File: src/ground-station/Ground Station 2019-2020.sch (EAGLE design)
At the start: 17 parts, among them U1 ADAFRUIT_RFM95W_LORA_RADIO

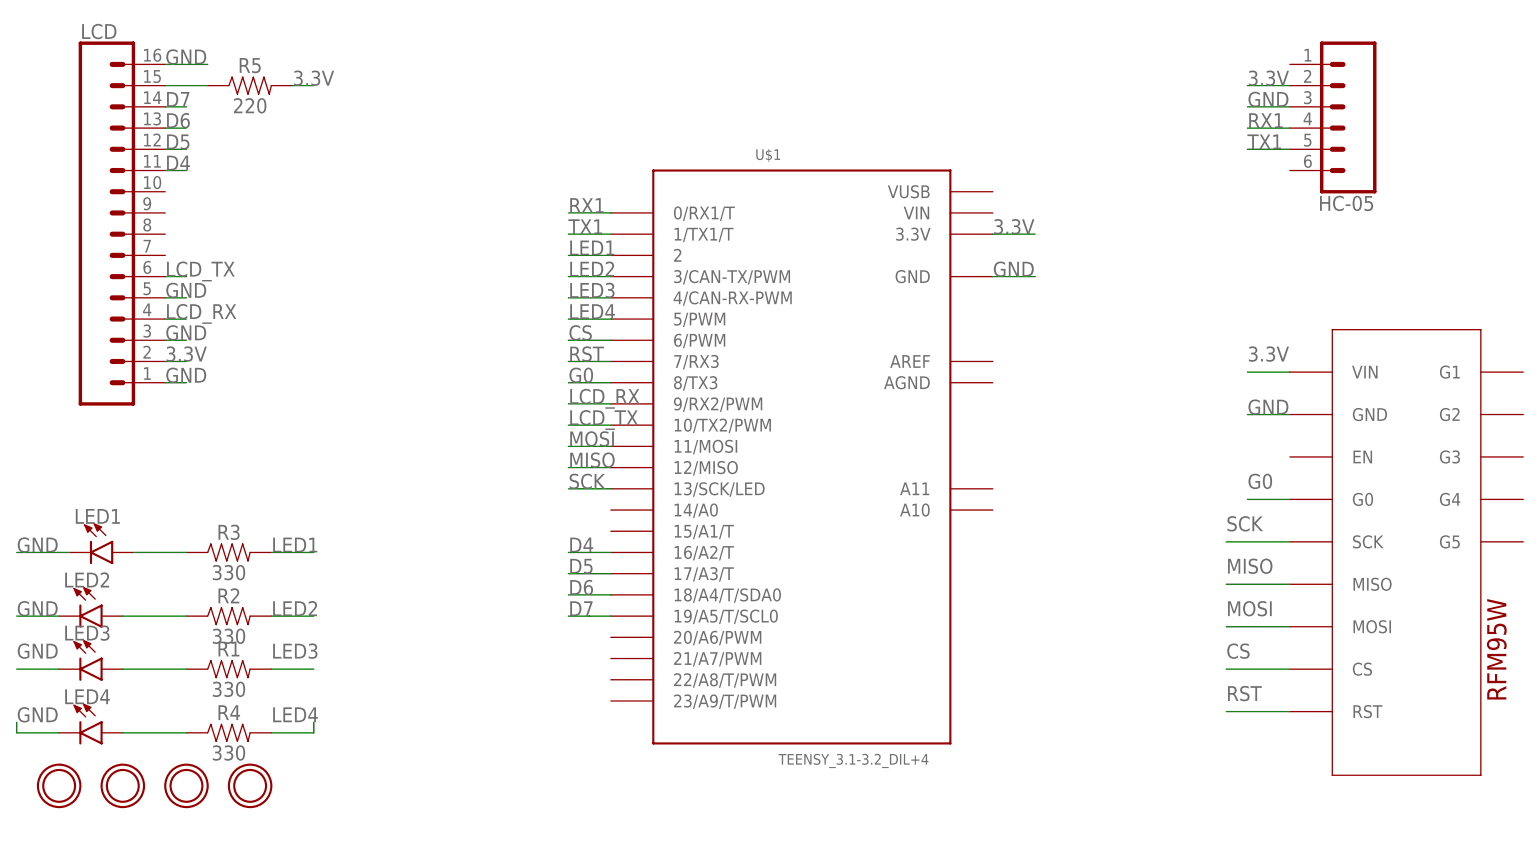
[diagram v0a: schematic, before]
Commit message: Changed LCD to OLED display, changed mounting holes.
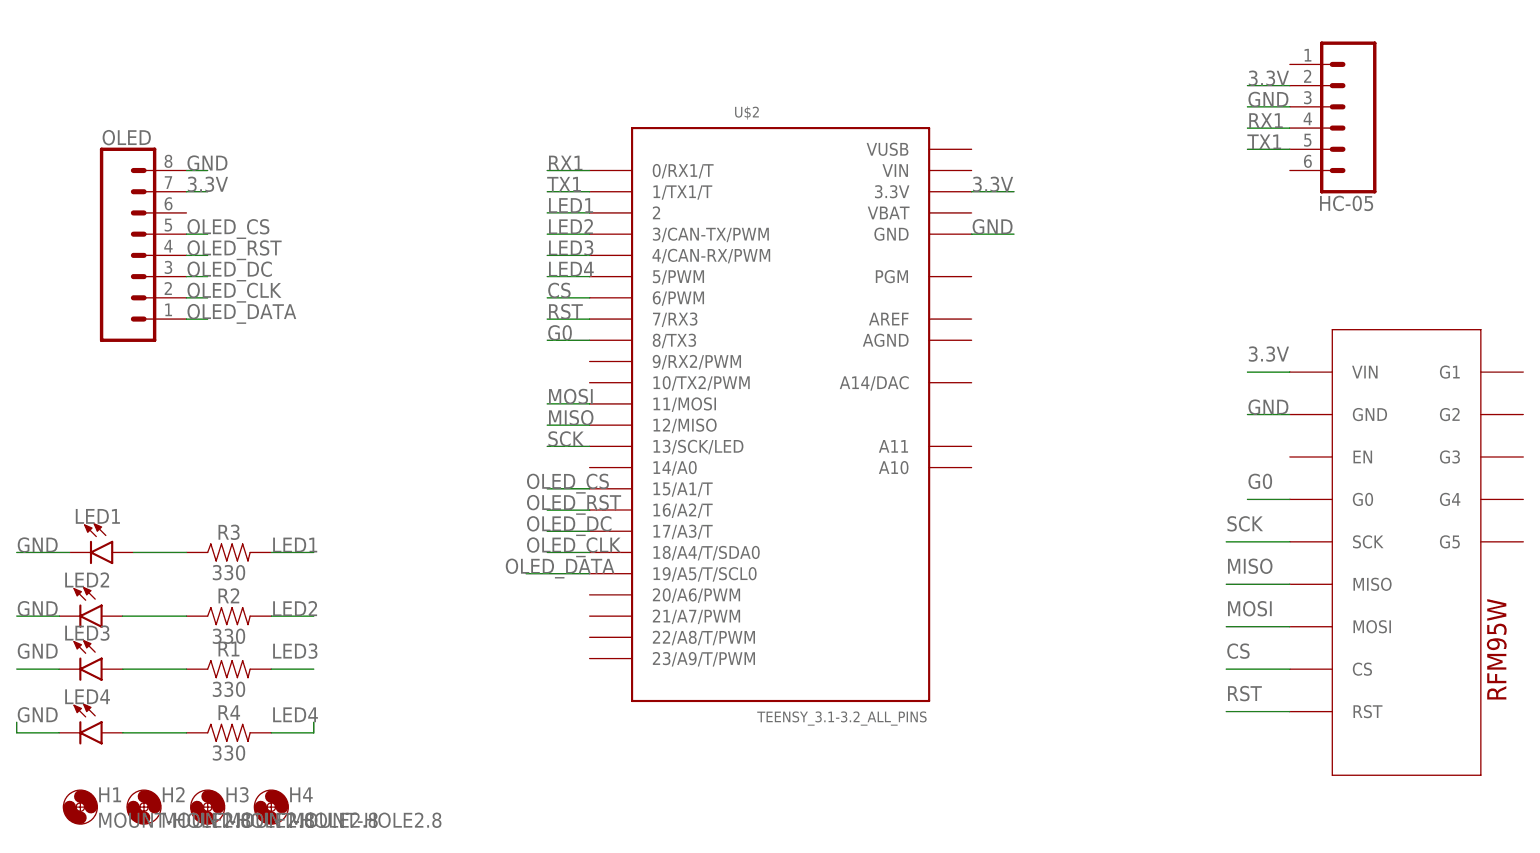
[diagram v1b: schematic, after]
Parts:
- removed LCD: (no value), SparkFun-Connectors:CONN_16
- removed R5: 220, SparkFun-Resistors:330OHM-HORIZ-1/10W-5%
- removed U$1: TEENSY_3.1-3.2_DIL+4, Teensy_3_and_LC_Series_Boards_v1.4:TEENSY_3.1-3.2_DIL+4
- removed U$3, U$4, U$5: MOUNTINGHOLE2.5, microbuilder:MOUNTINGHOLE2.5
- added H1, H2, H3, H4: MOUNT-HOLE2.8, holes:MOUNT-HOLE2.8
- added OLED: (no value), SparkFun-Connectors:CONN_08"
- U$2: value MOUNTINGHOLE2.5 -> TEENSY_3.1-3.2_ALL_PINS; device microbuilder:MOUNTINGHOLE2.5 -> Teensy_3_and_LC_Series_Boards_v1.4:TEENSY_3.1-3.2_ALL_PINS
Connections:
- removed net D4: LCD.11, U$1.16/A2/T
- removed net D5: LCD.12, U$1.17/A3/T
- removed net D6: LCD.13, U$1.18/A4/T/SDA0
- removed net D7: LCD.14, U$1.19/A5/T/SCL0
- removed net LCD_RX: LCD.4, U$1.9/RX2/PWM
- removed net LCD_TX: LCD.6, U$1.10/TX2/PWM
- removed net N$4: LCD.15, R5.1
- new net OLED_CLK: OLED.2, U$2.18/A4/T/SDA0
- new net OLED_CS: OLED.5, U$2.15/A1/T
- new net OLED_DATA: OLED.1, U$2.19/A5/T/SCL0
- new net OLED_DC: OLED.3, U$2.17/A3/T
- new net OLED_RST: OLED.4, U$2.16/A2/T
- net 3.3V: now also OLED.7, U$2.3.3V; no longer LCD.2, R5.2, U$1.3.3V
- net CS: now also U$2.6/PWM; no longer U$1.6/PWM
- net G0: now also U$2.8/TX3; no longer U$1.8/TX3
- net GND: now also OLED.8, U$2.GND; no longer LCD.1, LCD.16, LCD.3, LCD.5, U$1.GND
- net LED1: now also U$2.2; no longer U$1.2
- net LED2: now also U$2.3/CAN-TX/PWM; no longer U$1.3/CAN-TX/PWM
- net LED3: now also U$2.4/CAN-RX/PWM; no longer U$1.4/CAN-RX-PWM
- net LED4: now also U$2.5/PWM; no longer U$1.5/PWM
- net MISO: now also U$2.12/MISO; no longer U$1.12/MISO
- net MOSI: now also U$2.11/MOSI; no longer U$1.11/MOSI
- net RST: now also U$2.7/RX3; no longer U$1.7/RX3
- net RX1: now also U$2.0/RX1/T; no longer U$1.0/RX1/T
- net SCK: now also U$2.13/SCK/LED; no longer U$1.13/SCK/LED
- net TX1: now also U$2.1/TX1/T; no longer U$1.1/TX1/T

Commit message: Added Cam outputs
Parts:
- R1, R2, R3, R4: value 330 -> 220
- renumbered LED1 to RED, LED2 to YELLOW, LED3 to BLUE, LED4 to WHITE
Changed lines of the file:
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@@
 <part name="U1" library="AERO_Eagle_Library" deviceset="ADAFRUIT_RFM95W_LORA_RADIO" device=""/>
 <part name="HC-05" library="SparkFun-Connectors" library_urn="urn:adsk.eagle:library:513" deviceset="CONN_06" device="SILK_FEMALE_PTH" package3d_urn="urn:adsk.eagle:package:38009/1"/>
-<part name="LED1" library="SparkFun-LED" library_urn="urn:adsk.eagle:library:529" deviceset="LED" device="5MM" package3d_urn="urn:adsk.eagle:package:39353/1"/>
-<part name="LED2" library="SparkFun-LED" library_urn="urn:adsk.eagle:library:529" deviceset="LED" device="5MM" package3d_urn="urn:adsk.eagle:package:39353/1"/>
-<part name="LED3" library="SparkFun-LED" library_urn="urn:adsk.eagle:library:529" deviceset="LED" device="5MM" package3d_urn="urn:adsk.eagle:package:39353/1"/>
-<part name="R1" library="SparkFun-Resistors" library_urn="urn:adsk.eagle:library:532" deviceset="330OHM" device="-HORIZ-1/10W-5%" package3d_urn="urn:adsk.eagle:package:39658/1" value="330"/>
-<part name="R2" library="SparkFun-Resistors" library_urn="urn:adsk.eagle:library:532" deviceset="330OHM" device="-HORIZ-1/10W-5%" package3d_urn="urn:adsk.eagle:package:39658/1" value="330"/>
-<part name="R3" library="SparkFun-Resistors" library_urn="urn:adsk.eagle:library:532" deviceset="330OHM" device="-HORIZ-1/10W-5%" package3d_urn="urn:adsk.eagle:package:39658/1" value="330"/>
-<part name="R4" library="SparkFun-Resistors" library_urn="urn:adsk.eagle:library:532" deviceset="330OHM" device="-HORIZ-1/10W-5%" package3d_urn="urn:adsk.eagle:package:39658/1" value="330"/>
-<part name="LED4" library="SparkFun-LED" library_urn="urn:adsk.eagle:library:529" deviceset="LED" device="5MM" package3d_urn="urn:adsk.eagle:package:39353/1"/>
+<part name="RED" library="SparkFun-LED" library_urn="urn:adsk.eagle:library:529" deviceset="LED" device="5MM" package3d_urn="urn:adsk.eagle:package:39353/1"/>
+<part name="YELLOW" library="SparkFun-LED" library_urn="urn:adsk.eagle:library:529" deviceset="LED" device="5MM" package3d_urn="urn:adsk.eagle:package:39353/1"/>
+<part name="BLUE" library="SparkFun-LED" library_urn="urn:adsk.eagle:library:529" deviceset="LED" device="5MM" package3d_urn="urn:adsk.eagle:package:39353/1"/>
+<part name="R1" library="SparkFun-Resistors" library_urn="urn:adsk.eagle:library:532" deviceset="330OHM" device="-HORIZ-1/10W-5%" package3d_urn="urn:adsk.eagle:package:39658/1" value="220"/>
+<part name="R2" library="SparkFun-Resistors" library_urn="urn:adsk.eagle:library:532" deviceset="330OHM" device="-HORIZ-1/10W-5%" package3d_urn="urn:adsk.eagle:package:39658/1" value="220"/>
+<part name="R3" library="SparkFun-Resistors" library_urn="urn:adsk.eagle:library:532" deviceset="330OHM" device="-HORIZ-1/10W-5%" package3d_urn="urn:adsk.eagle:package:39658/1" value="220"/>
+<part name="R4" library="SparkFun-Resistors" library_urn="urn:adsk.eagle:library:532" deviceset="330OHM" device="-HORIZ-1/10W-5%" package3d_urn="urn:adsk.eagle:package:39658/1" value="220"/>
+<part name="WHITE" library="SparkFun-LED" library_urn="urn:adsk.eagle:library:529" deviceset="LED" device="5MM" package3d_urn="urn:adsk.eagle:package:39353/1"/>
 <part name="H1" library="holes" library_urn="urn:adsk.eagle:library:237" deviceset="MOUNT-HOLE" device="2.8" package3d_urn="urn:adsk.eagle:package:14271/1"/>
 <part name="H2" library="holes" library_urn="urn:adsk.eagle:library:237" deviceset="MOUNT-HOLE" device="2.8" package3d_urn="urn:adsk.eagle:package:14271/1"/>
@@
 <instance part="U1" gate="G$1" x="187.96" y="120.65" rot="R270"/>
 <instance part="HC-05" gate="G$1" x="187.96" y="147.32" rot="R180"/>
-<instance part="LED1" gate="G$1" x="41.91" y="93.98" rot="R270"/>
-<instance part="LED2" gate="G$1" x="40.64" y="86.36" rot="R270"/>
-<instance part="LED3" gate="G$1" x="40.64" y="80.01" rot="R270"/>
+<instance part="RED" gate="G$1" x="41.91" y="93.98" rot="R270"/>
+<instance part="YELLOW" gate="G$1" x="40.64" y="86.36" rot="R270"/>
+<instance part="BLUE" gate="G$1" x="40.64" y="80.01" rot="R270"/>
 <instance part="R1" gate="G$1" x="55.88" y="80.01"/>
 <instance part="R2" gate="G$1" x="55.88" y="86.36"/>
 <instance part="R3" gate="G$1" x="55.88" y="93.98"/>
 <instance part="R4" gate="G$1" x="55.88" y="72.39"/>
-<instance part="LED4" gate="G$1" x="40.64" y="72.39" rot="R270"/>
+<instance part="WHITE" gate="G$1" x="40.64" y="72.39" rot="R270"/>
 <instance part="H1" gate="G$1" x="38.1" y="63.5"/>
 <instance part="H2" gate="G$1" x="45.72" y="63.5"/>
@@
 </segment>
 <segment>
-<pinref part="LED3" gate="G$1" pin="C"/>
+<pinref part="BLUE" gate="G$1" pin="C"/>
 <wire x1="35.56" y1="80.01" x2="30.48" y2="80.01" width="0.1524" layer="91"/>
 <label x="30.48" y="81.28" size="1.778" layer="95"/>
 </segment>
 <segment>
-<pinref part="LED2" gate="G$1" pin="C"/>
+<pinref part="YELLOW" gate="G$1" pin="C"/>
 <wire x1="35.56" y1="86.36" x2="30.48" y2="86.36" width="0.1524" layer="91"/>
 <label x="30.48" y="86.36" size="1.778" layer="95"/>
 </segment>
 <segment>
-<pinref part="LED1" gate="G$1" pin="C"/>
+<pinref part="RED" gate="G$1" pin="C"/>
 <wire x1="36.83" y1="93.98" x2="30.48" y2="93.98" width="0.1524" layer="91"/>
 <label x="30.48" y="93.98" size="1.778" layer="95"/>
@@
 </segment>
 <segment>
-<pinref part="LED4" gate="G$1" pin="C"/>
+<pinref part="WHITE" gate="G$1" pin="C"/>
 <wire x1="35.56" y1="72.39" x2="30.48" y2="72.39" width="0.1524" layer="91"/>
 <wire x1="30.48" y1="72.39" x2="30.48" y2="73.66" width="0.1524" layer="91"/>
@@
 <segment>
 <pinref part="R1" gate="G$1" pin="1"/>
-<pinref part="LED3" gate="G$1" pin="A"/>
+<pinref part="BLUE" gate="G$1" pin="A"/>
 <wire x1="50.8" y1="80.01" x2="43.18" y2="80.01" width="0.1524" layer="91"/>
 </segment>
@@
 <segment>
 <pinref part="R2" gate="G$1" pin="1"/>
-<pinref part="LED2" gate="G$1" pin="A"/>
+<pinref part="YELLOW" gate="G$1" pin="A"/>
 <wire x1="50.8" y1="86.36" x2="43.18" y2="86.36" width="0.1524" layer="91"/>
 </segment>
@@
 <segment>
 <pinref part="R3" gate="G$1" pin="1"/>
-<pinref part="LED1" gate="G$1" pin="A"/>
+<pinref part="RED" gate="G$1" pin="A"/>
 <wire x1="50.8" y1="93.98" x2="44.45" y2="93.98" width="0.1524" layer="91"/>
 </segment>
@@
 <net name="N$5" class="0">
 <segment>
-<pinref part="LED4" gate="G$1" pin="A"/>
+<pinref part="WHITE" gate="G$1" pin="A"/>
 <pinref part="R4" gate="G$1" pin="1"/>
 <wire x1="43.18" y1="72.39" x2="50.8" y2="72.39" width="0.1524" layer="91"/>
